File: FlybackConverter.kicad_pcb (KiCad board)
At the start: 2 copper layers, 76.2 x 76.2 mm, 46 parts, among them J1 USB_C_Receptacle_PowerOnly_6P, T1 Transformer_1P_2S, U1 LNK6428K, U2 TPS25820DSST

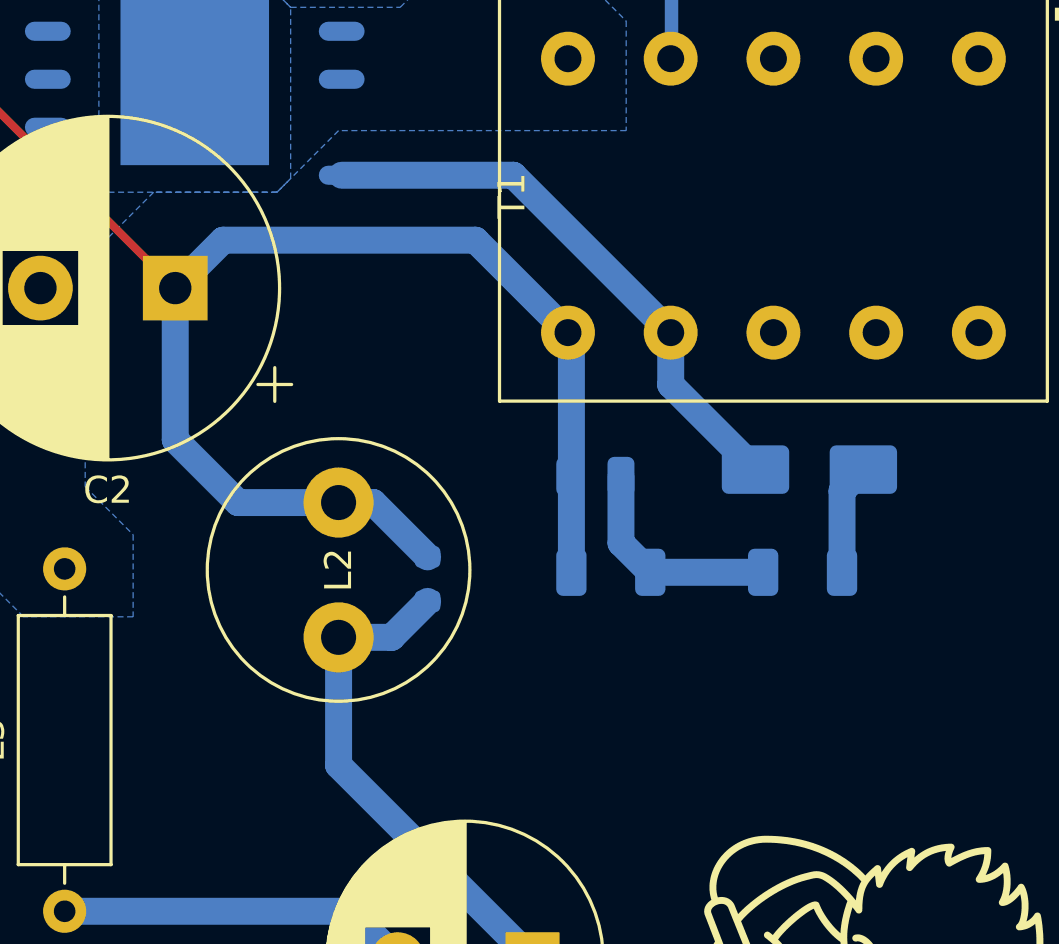
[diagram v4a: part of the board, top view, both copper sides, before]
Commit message: スナバ配置変更 fix #8
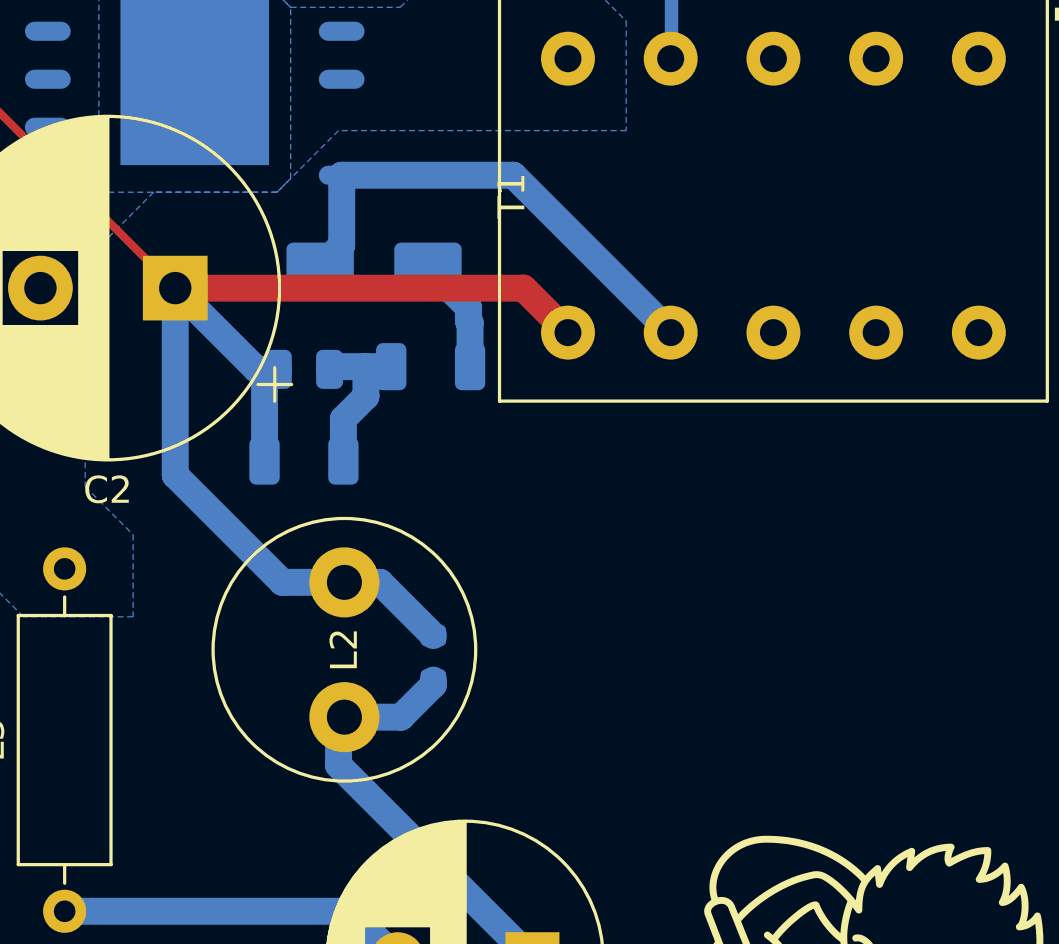
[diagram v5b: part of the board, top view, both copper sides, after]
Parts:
- moved D2 17.8 mm to (152.7, 77.7)
- moved R3 15.8 mm to (154.8, 81.4)
- moved R11 12.1 mm to (150.1, 84.9)
- moved C6 11.5 mm to (150.1, 81.5)
- moved L2 2.97 mm to (151.6, 94.4)
- moved R10 2.93 mm to (154.9, 92.2)
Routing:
- net Net-(BR1-+): track 26.6 -> 23.8 mm
- net Net-(D2-A): track 21.0 -> 18.4 mm
- net Net-(C6-Pad2): track 8.19 -> 6.18 mm
- net Net-(T1-AA): track 59.1 -> 59.8 mm
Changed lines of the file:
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@@
   )
   (footprint "Inductor_THT:L_Radial_D9.5mm_P5.00mm_Fastron_07HVP" (layer "F.Cu")
-    (at 151.384 91.44 90)
+    (at 151.6 94.4 90)
     (descr "Inductor, Radial series, Radial, pin pitch=5.00mm, , diameter=9.5mm, Fastron, 07HVP, http://www.fastrongroup.com/image-show/107/07HVP%2007HVP_T.pdf?type=Complete-DataSheet&productType=series")
     (tags "Inductor Radial series Radial pin pitch 5.00mm  diameter 9.5mm Fastron 07HVP")
@@
   )
   (footprint "Resistor_SMD:R_0603_1608Metric" (layer "B.Cu")
-    (at 154.686 89.281 90)
+    (at 154.9 92.2 90)
     (descr "Resistor SMD 0603 (1608 Metric), square (rectangular) end terminal, IPC_7351 nominal, (Body size source: IPC-SM-782 page 72, https://www.pcb-3d.com/wordpress/wp-content/uploads/ipc-sm-782a_amendment_1_and_2.pdf), generated with kicad-footprint-generator")
     (tags "resistor")
@@
   )
   (footprint "Diode_SMD:D_SMA" (layer "B.Cu")
-    (at 168.8485 85.217 180)
+    (at 152.7 77.7 180)
     (descr "Diode SMA (DO-214AC)")
     (tags "Diode SMA (DO-214AC)")
@@
   )
   (footprint "Resistor_SMD:R_1206_3216Metric" (layer "B.Cu")
-    (at 168.5945 89.027)
+    (at 154.8 81.4)
     (descr "Resistor SMD 1206 (3216 Metric), square (rectangular) end terminal, IPC_7351 nominal, (Body size source: IPC-SM-782 page 72, https://www.pcb-3d.com/wordpress/wp-content/uploads/ipc-sm-782a_amendment_1_and_2.pdf), generated with kicad-footprint-generator")
     (tags "resistor")
@@
   )
   (footprint "Resistor_SMD:R_1206_3216Metric" (layer "B.Cu")
-    (at 161.4825 89.027)
+    (at 150.1 84.9)
     (descr "Resistor SMD 1206 (3216 Metric), square (rectangular) end terminal, IPC_7351 nominal, (Body size source: IPC-SM-782 page 72, https://www.pcb-3d.com/wordpress/wp-content/uploads/ipc-sm-782a_amendment_1_and_2.pdf), generated with kicad-footprint-generator")
     (tags "resistor")
@@
   )
   (footprint "Capacitor_SMD:C_0805_2012Metric" (layer "B.Cu")
-    (at 160.909 85.471)
+    (at 150.1 81.5)
     (descr "Capacitor SMD 0805 (2012 Metric), square (rectangular) end terminal, IPC_7351 nominal, (Body size source: IPC-SM-782 page 76, https://www.pcb-3d.com/wordpress/wp-content/uploads/ipc-sm-782a_amendment_1_and_2.pdf, https://docs.google.com/spreadsheets/d/1BsfQQcO9C6DZCsRaXUlFlo91Tg2WpOkGARC1WS5S8t0/edit?usp=sharing), generated with kicad-footprint-generator")
     (tags "capacitor")
@@
     (effects (font (size 1.5 1.5) (thickness 0.15)))
   )
-  (segment (start 151.384 91.44) (end 151.384 96.184323) (width 1) (layer "B.Cu") (net 1))
-  (segment (start 151.384 96.184323) (end 158.577677 103.378) (width 1) (layer "B.Cu") (net 1))
-  (segment (start 153.352 91.44) (end 154.686 90.106) (width 1) (layer "B.Cu") (net 1))
+  (segment (start 154.9 93.2) (end 154.9 93.025) (width 1) (layer "B.Cu") (net 1))
+  (segment (start 151.6 94.4) (end 153.7 94.4) (width 1) (layer "B.Cu") (net 1))
+  (segment (start 153.7 94.4) (end 154.9 93.2) (width 1) (layer "B.Cu") (net 1))
   (segment (start 158.777 103.577323) (end 158.777 110.998) (width 1) (layer "B.Cu") (net 1))
+  (segment (start 151.384 94.616) (end 151.384 96.184323) (width 1) (layer "B.Cu") (net 1))
+  (segment (start 151.6 94.4) (end 151.384 94.616) (width 1) (layer "B.Cu") (net 1))
   (segment (start 158.577677 103.378) (end 158.640677 103.441) (width 1) (layer "B.Cu") (net 1))
   (segment (start 158.577677 103.378) (end 158.777 103.577323) (width 1) (layer "B.Cu") (net 1))
-  (segment (start 151.384 91.44) (end 153.352 91.44) (width 1) (layer "B.Cu") (net 1))
+  (segment (start 151.384 96.184323) (end 158.577677 103.378) (width 1) (layer "B.Cu") (net 1))
   (segment (start 151.799677 101.6) (end 153.577677 103.378) (width 1) (layer "B.Cu") (net 2))
   (segment (start 155.448 105.248323) (end 153.577677 103.378) (width 1) (layer "B.Cu") (net 2))
@@
   (segment (start 150.595 108.966) (end 152.627 110.998) (width 1.5) (layer "B.Cu") (net 4))
   (segment (start 131.826 70.866) (end 137.705959 70.866) (width 0.3) (layer "F.Cu") (net 5))
+  (segment (start 145.26998 78.430021) (end 145.26998 78.43002) (width 0.3) (layer "F.Cu") (net 5))
+  (segment (start 145.325959 78.486) (end 158.242 78.486) (width 1) (layer "F.Cu") (net 5))
+  (segment (start 158.242 78.486) (end 159.893 80.137) (width 1) (layer "F.Cu") (net 5))
+  (segment (start 145.325959 78.486) (end 145.26998 78.430021) (width 0.3) (layer "F.Cu") (net 5))
   (segment (start 137.705959 70.866) (end 145.325959 78.486) (width 0.3) (layer "F.Cu") (net 5))
-  (segment (start 156.464 76.708) (end 159.893 80.137) (width 1) (layer "B.Cu") (net 5))
-  (segment (start 152.67 86.44) (end 154.686 88.456) (width 1) (layer "B.Cu") (net 5))
-  (segment (start 151.384 86.44) (end 152.67 86.44) (width 1) (layer "B.Cu") (net 5))
-  (segment (start 151.384 86.44) (end 147.654 86.44) (width 1) (layer "B.Cu") (net 5))
-  (segment (start 160.02 80.264) (end 160.02 89.027) (width 1) (layer "B.Cu") (net 5))
-  (segment (start 145.325959 84.111959) (end 145.325959 78.486) (width 1) (layer "B.Cu") (net 5))
-  (segment (start 145.325959 78.486) (end 147.103959 76.708) (width 1) (layer "B.Cu") (net 5))
-  (segment (start 147.654 86.44) (end 145.325959 84.111959) (width 1) (layer "B.Cu") (net 5))
+  (segment (start 145.325959 85.425959) (end 145.325959 78.486) (width 1) (layer "B.Cu") (net 5))
+  (segment (start 151.6 89.4) (end 149.3 89.4) (width 1) (layer "B.Cu") (net 5))
+  (segment (start 151.6 89.4) (end 152.925 89.4) (width 1) (layer "B.Cu") (net 5))
+  (segment (start 149.15 81.5) (end 148.6375 82.0125) (width 1) (layer "B.Cu") (net 5))
+  (segment (start 152.925 89.4) (end 154.9 91.375) (width 1) (layer "B.Cu") (net 5))
   (segment (start 159.893 80.137) (end 160.02 80.264) (width 1) (layer "B.Cu") (net 5))
-  (segment (start 147.103959 76.708) (end 156.464 76.708) (width 1) (layer "B.Cu") (net 5))
+  (segment (start 149.15 81.5) (end 148.339959 81.5) (width 1) (layer "B.Cu") (net 5))
+  (segment (start 149.3 89.4) (end 145.325959 85.425959) (width 1) (layer "B.Cu") (net 5))
+  (segment (start 148.6375 82.0125) (end 148.6375 84.9) (width 1) (layer "B.Cu") (net 5))
+  (segment (start 148.339959 81.5) (end 145.325959 78.486) (width 1) (layer "B.Cu") (net 5))
   (segment (start 195.596 62.722) (end 193.294 65.024) (width 1.5) (layer "B.Cu") (net 6))
   (segment (start 195.596 60.548) (end 195.596 62.722) (width 1.5) (layer "B.Cu") (net 6))
@@
   (segment (start 193.294 74.908) (end 193.294 65.024) (width 0.5) (layer "B.Cu") (net 6))
   (segment (start 193.696 60.548) (end 191.2405 60.548) (width 1.5) (layer "B.Cu") (net 7))
-  (segment (start 161.859 85.471) (end 161.859 87.941) (width 1) (layer "B.Cu") (net 8))
-  (segment (start 162.945 89.027) (end 167.132 89.027) (width 1) (layer "B.Cu") (net 8))
-  (segment (start 161.859 87.941) (end 162.945 89.027) (width 1) (layer "B.Cu") (net 8))
+  (segment (start 153.3375 81.4) (end 152.4 81.4) (width 1) (layer "B.Cu") (net 8))
+  (segment (start 152.4 81.4) (end 152.4 82.5) (width 1) (layer "B.Cu") (net 8))
+  (segment (start 152.4 82.5) (end 151.5625 83.3375) (width 1) (layer "B.Cu") (net 8))
+  (segment (start 151.15 81.4) (end 151.05 81.5) (width 1) (layer "B.Cu") (net 8))
+  (segment (start 151.5625 83.3375) (end 151.5625 84.9) (width 1) (layer "B.Cu") (net 8))
+  (segment (start 152.4 81.4) (end 151.15 81.4) (width 1) (layer "B.Cu") (net 8))
   (segment (start 151.575 62.23) (end 148.541 62.23) (width 0.5) (layer "B.Cu") (net 9))
   (segment (start 148.541 62.23) (end 148.541 64.475) (width 0.5) (layer "B.Cu") (net 9))
@@
   (segment (start 153.225 61.785) (end 153.225 62.23) (width 0.5) (layer "B.Cu") (net 10))
   (segment (start 151.081 58.674) (end 151.081 59.641) (width 0.5) (layer "B.Cu") (net 10))
-  (segment (start 170.057 89.027) (end 170.057 86.0085) (width 1) (layer "B.Cu") (net 11))
-  (segment (start 170.057 86.0085) (end 170.8485 85.217) (width 1) (layer "B.Cu") (net 11))
-  (segment (start 163.703 80.137) (end 163.703 82.0715) (width 1) (layer "B.Cu") (net 12))
+  (segment (start 156.2625 79.7625) (end 156.2625 81.4) (width 1) (layer "B.Cu") (net 11))
+  (segment (start 154.7 77.7) (end 156.2 79.2) (width 1) (layer "B.Cu") (net 11))
+  (segment (start 156.2 79.7) (end 156.2625 79.7625) (width 1) (layer "B.Cu") (net 11))
+  (segment (start 156.2 79.2) (end 156.2 79.7) (width 1) (layer "B.Cu") (net 11))
+  (segment (start 151.5 74.3) (end 151.5 76.9) (width 1) (layer "B.Cu") (net 12))
   (segment (start 151.5 74.3) (end 157.866 74.3) (width 1) (layer "B.Cu") (net 12))
   (segment (start 157.866 74.3) (end 163.703 80.137) (width 1) (layer "B.Cu") (net 12))
-  (segment (start 163.703 82.0715) (end 166.8485 85.217) (width 1) (layer "B.Cu") (net 12))
+  (segment (start 151.5 76.9) (end 150.7 77.7) (width 1) (layer "B.Cu") (net 12))
   (segment (start 163.83 62.621) (end 161.724 60.515) (width 0.5) (layer "B.Cu") (net 13))
   (segment (start 163.83 64.008) (end 163.83 62.621) (width 0.5) (layer "B.Cu") (net 13))

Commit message: トランス周辺のネット名変更
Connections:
- net Net-(T1-AA) renamed PRI
- net Net-(T1-SA) renamed FB
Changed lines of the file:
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@@
   (net 3 "Net-(BR1-Pad3)")
   (net 4 "Net-(BR1-Pad4)")
-  (net 5 "Net-(T1-AA)")
+  (net 5 "PRI")
   (net 6 "Net-(D1-K)")
   (net 7 "Net-(C5-Pad1)")
@@
   (net 18 "FL2")
   (net 19 "FL1")
-  (net 20 "Net-(T1-SA)")
+  (net 20 "FB")
   (net 21 "5V")
   (net 22 "Net-(U2-REF)")
@@
       (stroke (width 0.12) (type solid)) (fill none) (layer "F.Fab"))
     (pad "1" thru_hole circle (at 0 0) (size 2 2) (drill 1) (layers "*.Cu" "*.Mask")
-      (net 5 "Net-(T1-AA)") (pinfunction "1") (pintype "passive"))
+      (net 5 "PRI") (pinfunction "1") (pintype "passive"))
     (model "${KICAD6_3DMODEL_DIR}/TestPoint.3dshapes/TestPoint_Loop_D1.80mm_Drill1.0mm_Beaded.wrl"
       (offset (xyz 0 0 0))
@@
       (stroke (width 0.1) (type solid)) (fill none) (layer "F.Fab"))
     (pad "1" thru_hole rect (at 0 0 180) (size 2.4 2.4) (drill 1.2) (layers "*.Cu" "*.Mask")
-      (net 5 "Net-(T1-AA)") (pintype "passive"))
+      (net 5 "PRI") (pintype "passive"))
     (pad "2" thru_hole circle (at 5 0 180) (size 2.4 2.4) (drill 1.2) (layers "*.Cu" "*.Mask")
       (net 17 "Net-(T1-SB)") (pintype "passive"))
@@
     (pad "3" thru_hole circle (at -5.08 0 90) (size 2 2) (drill 1) (layers "*.Cu" "*.Mask"))
     (pad "4" thru_hole circle (at -5.08 3.81 90) (size 2 2) (drill 1) (layers "*.Cu" "*.Mask")
-      (net 20 "Net-(T1-SA)") (pinfunction "SA") (pintype "passive"))
+      (net 20 "FB") (pinfunction "SA") (pintype "passive"))
     (pad "5" thru_hole circle (at -5.08 7.62 90) (size 2 2) (drill 1) (layers "*.Cu" "*.Mask")
       (net 17 "Net-(T1-SB)") (pinfunction "SB") (pintype "passive"))
     (pad "6" thru_hole circle (at 5.08 7.62 90) (size 2 2) (drill 1) (layers "*.Cu" "*.Mask")
-      (net 5 "Net-(T1-AA)") (pinfunction "AA") (pintype "passive"))
+      (net 5 "PRI") (pinfunction "AA") (pintype "passive"))
     (pad "7" thru_hole circle (at 5.08 3.81 90) (size 2 2) (drill 1) (layers "*.Cu" "*.Mask")
       (net 12 "Net-(D2-A)") (pinfunction "AB") (pintype "passive"))
@@
       (net 1 "Net-(BR1-+)") (pinfunction "1") (pintype "passive"))
     (pad "2" thru_hole circle (at 5 0 90) (size 2.6 2.6) (drill 1.3) (layers "*.Cu" "*.Mask")
-      (net 5 "Net-(T1-AA)") (pinfunction "2") (pintype "passive"))
+      (net 5 "PRI") (pinfunction "2") (pintype "passive"))
     (model "${KICAD6_3DMODEL_DIR}/Inductor_THT.3dshapes/L_Radial_D9.5mm_P5.00mm_Fastron_07HVP.wrl"
       (offset (xyz 0 0 0))
@@
       (stroke (width 0.12) (type solid)) (fill none) (layer "F.Fab"))
     (pad "1" thru_hole circle (at 0 0) (size 2 2) (drill 1) (layers "*.Cu" "*.Mask")
-      (net 20 "Net-(T1-SA)") (pinfunction "1") (pintype "passive"))
+      (net 20 "FB") (pinfunction "1") (pintype "passive"))
     (model "${KICAD6_3DMODEL_DIR}/TestPoint.3dshapes/TestPoint_Loop_D1.80mm_Drill1.0mm_Beaded.wrl"
       (offset (xyz 0 0 0))
@@
       (net 1 "Net-(BR1-+)") (pintype "passive"))
     (pad "2" smd roundrect (at 0.825 0 90) (size 0.8 0.95) (layers "B.Cu" "B.Paste" "B.Mask") (roundrect_rratio 0.25)
-      (net 5 "Net-(T1-AA)") (pintype "passive"))
+      (net 5 "PRI") (pintype "passive"))
     (model "${KICAD6_3DMODEL_DIR}/Resistor_SMD.3dshapes/R_0603_1608Metric.wrl"
       (offset (xyz 0 0 0))
@@
       (stroke (width 0.1) (type solid)) (layer "B.Fab"))
     (pad "1" smd roundrect (at -0.825 0 90) (size 0.8 0.95) (layers "B.Cu" "B.Paste" "B.Mask") (roundrect_rratio 0.25)
-      (net 20 "Net-(T1-SA)") (pintype "passive"))
+      (net 20 "FB") (pintype "passive"))
     (pad "2" smd roundrect (at 0.825 0 90) (size 0.8 0.95) (layers "B.Cu" "B.Paste" "B.Mask") (roundrect_rratio 0.25)
       (net 13 "Net-(D3-A)") (pintype "passive"))
@@
       (stroke (width 0.1) (type solid)) (layer "B.Fab"))
     (pad "1" smd roundrect (at -1.4625 0) (size 1.125 1.75) (layers "B.Cu" "B.Paste" "B.Mask") (roundrect_rratio 0.222222)
-      (net 5 "Net-(T1-AA)") (pintype "passive"))
+      (net 5 "PRI") (pintype "passive"))
     (pad "2" smd roundrect (at 1.4625 0) (size 1.125 1.75) (layers "B.Cu" "B.Paste" "B.Mask") (roundrect_rratio 0.222222)
       (net 8 "Net-(C6-Pad2)") (pintype "passive"))
@@
       (stroke (width 0.1) (type solid)) (layer "B.Fab"))
     (pad "1" smd roundrect (at -0.825 0 90) (size 0.8 0.95) (layers "B.Cu" "B.Paste" "B.Mask") (roundrect_rratio 0.25)
-      (net 20 "Net-(T1-SA)") (pintype "passive"))
+      (net 20 "FB") (pintype "passive"))
     (pad "2" smd roundrect (at 0.825 0 90) (size 0.8 0.95) (layers "B.Cu" "B.Paste" "B.Mask") (roundrect_rratio 0.25)
       (net 15 "Net-(U1-FB)") (pintype "passive"))
@@
       (stroke (width 0.1) (type solid)) (layer "B.Fab"))
     (pad "1" smd roundrect (at -0.95 0) (size 1 1.45) (layers "B.Cu" "B.Paste" "B.Mask") (roundrect_rratio 0.25)
-      (net 5 "Net-(T1-AA)") (pintype "passive"))
+      (net 5 "PRI") (pintype "passive"))
     (pad "2" smd roundrect (at 0.95 0) (size 1 1.45) (layers "B.Cu" "B.Paste" "B.Mask") (roundrect_rratio 0.25)
       (net 8 "Net-(C6-Pad2)") (pintype "passive"))
